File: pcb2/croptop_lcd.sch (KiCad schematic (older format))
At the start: 110 parts, among them J5 D.N.P., J6 686104183422, J7 62684-402100ALF, Q1 BSS138, Q2 BSS138, U11 TPD4E1U06, U12 FT812Q, U13 TPD4E1U06, U14 TPD4E1U06, U15 TPD4E1U06, U16 TPD4E1U06, U17 TPD4E1U06, U18 TPD4E1U06, U19 TPD4E1U06, U20 TPD4E1U06, Y2 ABLS-12.000MHZ-B2-T

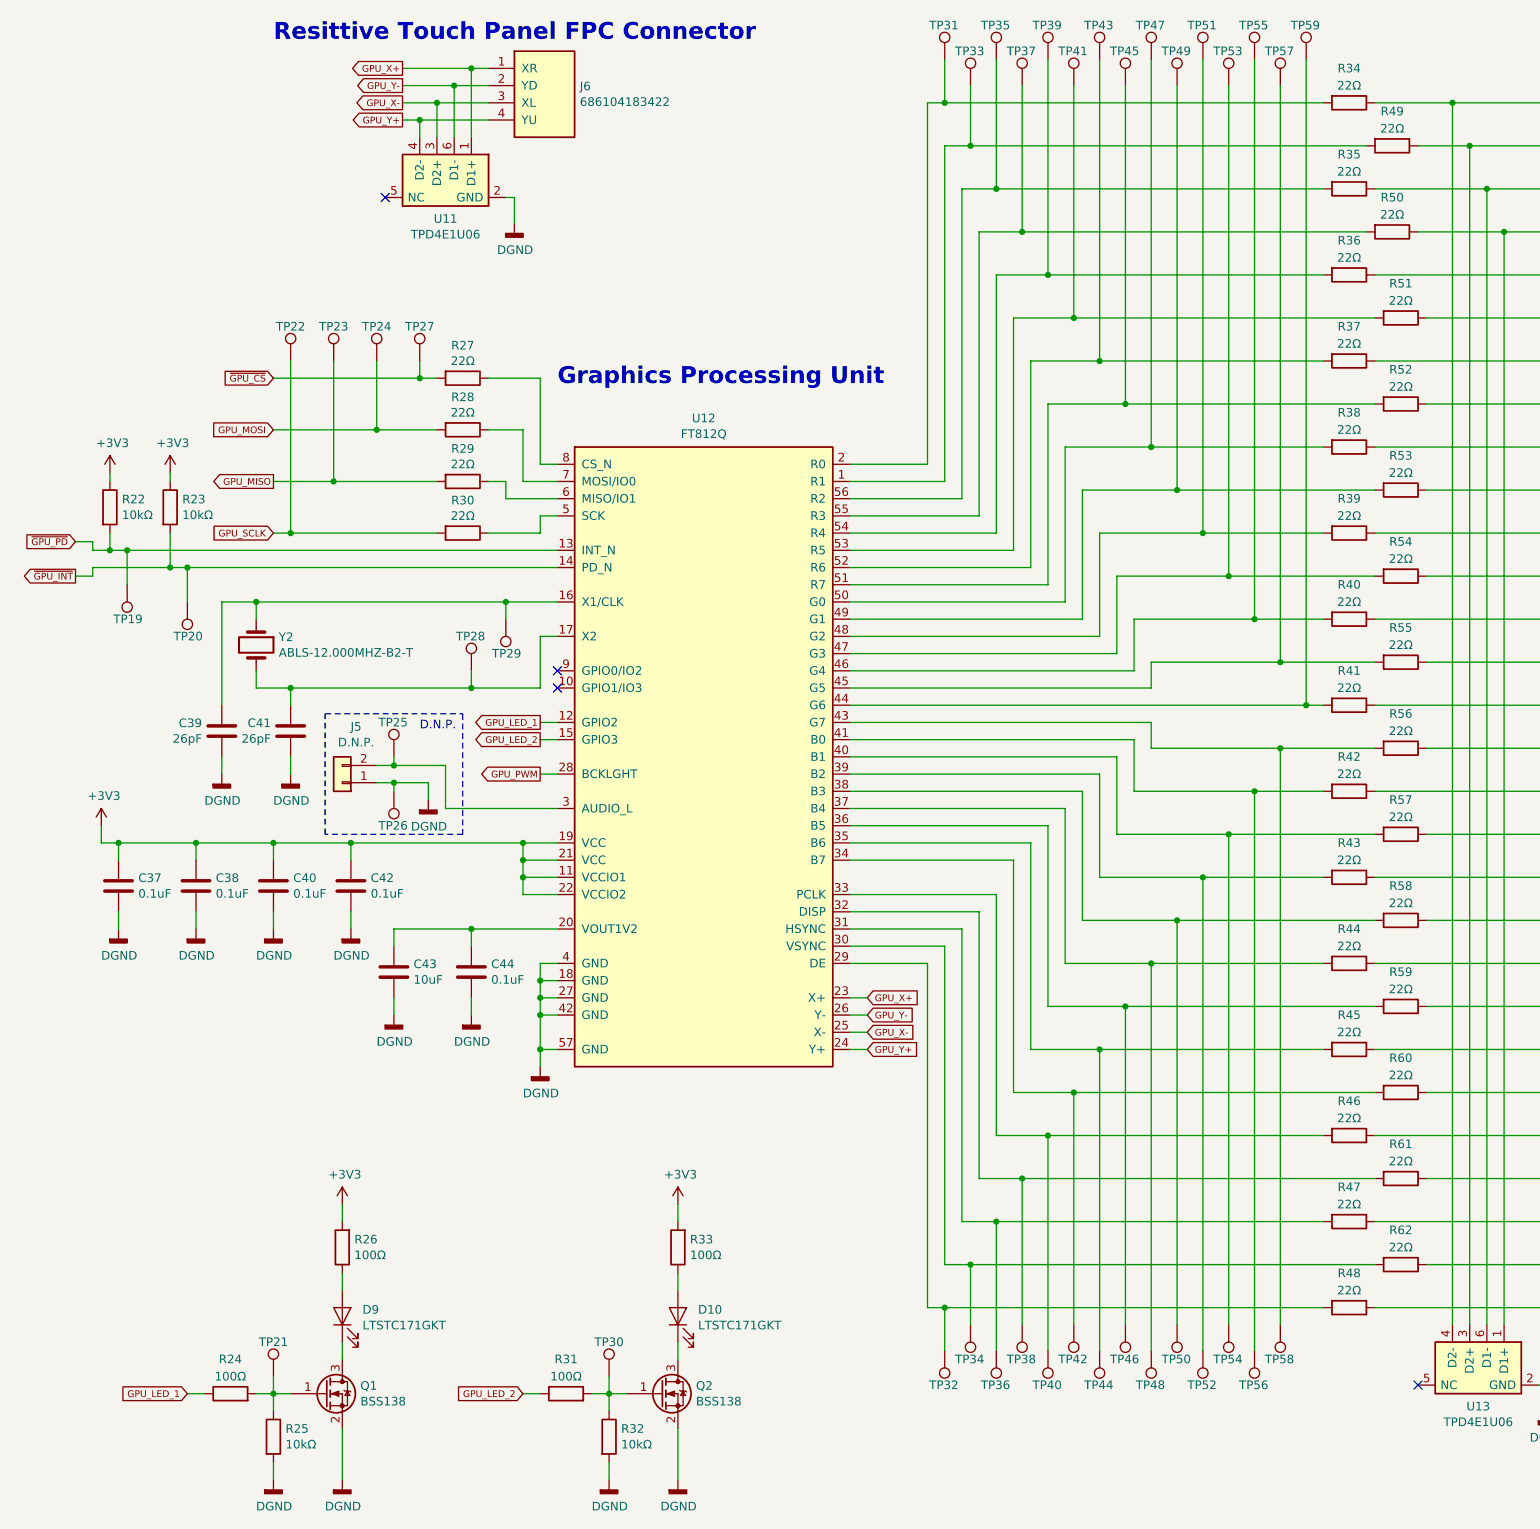
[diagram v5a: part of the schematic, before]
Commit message: Updated pin out
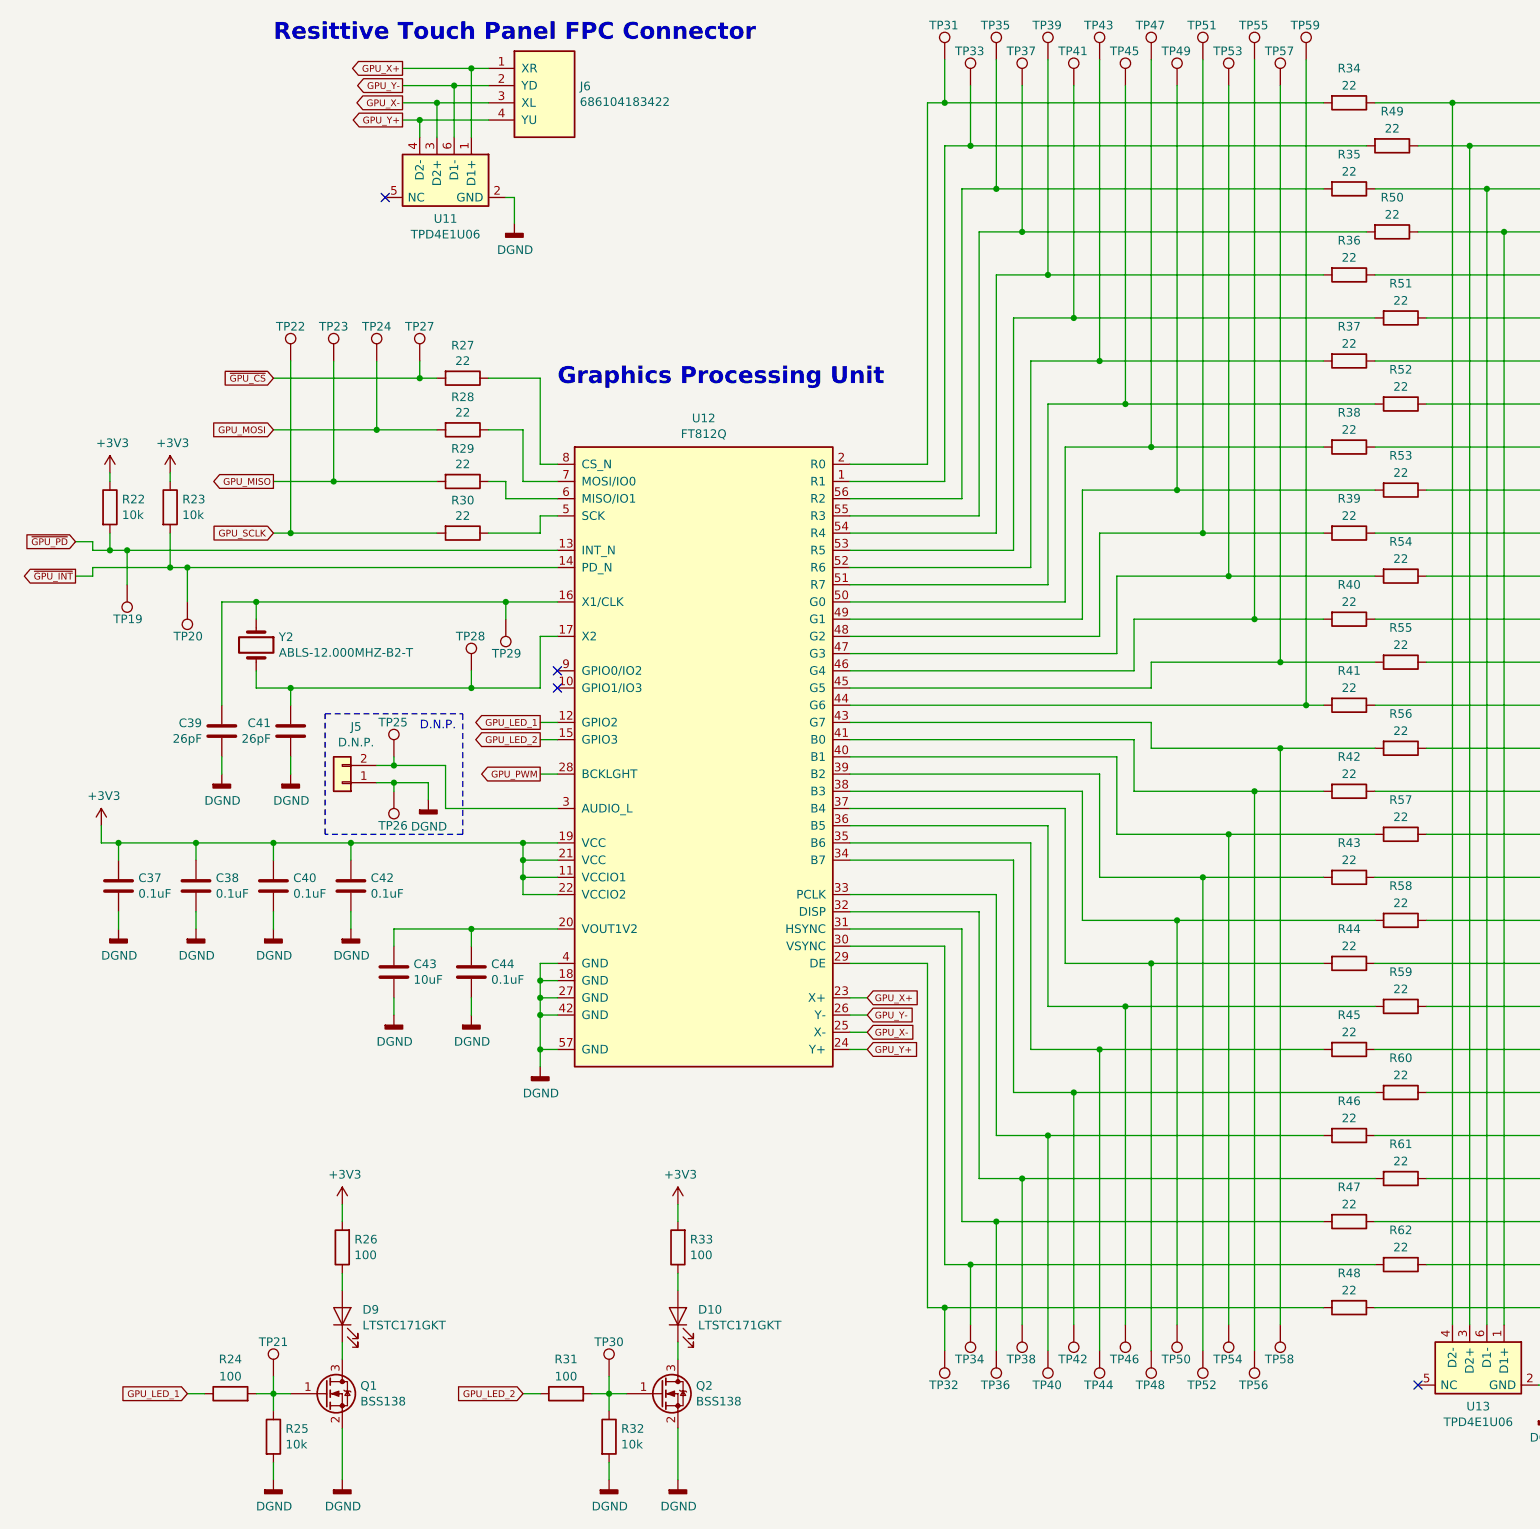
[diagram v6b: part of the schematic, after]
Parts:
- R22, R23, R25, R32: value 10kΩ -> 10k
- R24, R26, R31, R33: value 100Ω -> 100
- R27, R28, R29, R30, R34, R35, R36, R37, R38, R39, R40, R41, R42, R43, R44, R45, R46, R47, R48, R49, R50, R51, R52, R53, R54, R55, R56, R57, R58, R59, R60, R61, R62: value 22Ω -> 22
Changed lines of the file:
@@
 $Descr USLedger 17000 11000
 encoding utf-8
-Sheet 4 6
+Sheet 3 5
 Title "CropTop 2.0"
 Date "2019-03-18"
@@
 P 1150 3850
 F 0 "R22" H 1220 3896 50  0000 L CNN
-F 1 "10kΩ" H 1220 3805 50  0000 L CNN
+F 1 "10k" H 1220 3805 50  0000 L CNN
 F 2 "Resistor_SMD:R_0402_1005Metric" V 1080 3850 50  0001 C CNN
 F 3 "" H 1150 3850 50  0001 C CNN
@@
 P 1500 3850
 F 0 "R23" H 1570 3896 50  0000 L CNN
-F 1 "10kΩ" H 1570 3805 50  0000 L CNN
+F 1 "10k" H 1570 3805 50  0000 L CNN
 F 2 "Resistor_SMD:R_0402_1005Metric" V 1430 3850 50  0001 C CNN
 F 3 "" H 1500 3850 50  0001 C CNN
@@
 AR Path="/65B709D0/5CF1E28C" Ref="R30"  Part="1"
 F 0 "R30" V 3010 4000 50  0000 C CNN
-F 1 "22Ω" V 3100 4000 50  0000 C CNN
+F 1 "22" V 3100 4000 50  0000 C CNN
 F 2 "Resistor_SMD:R_0402_1005Metric" V 3130 4000 50  0001 C CNN
 F 3 "" H 3200 4000 50  0001 C CNN
@@
 AR Path="/65B709D0/5CF1E293" Ref="R29"  Part="1"
 F 0 "R29" V 3010 3700 50  0000 C CNN
-F 1 "22Ω" V 3100 3700 50  0000 C CNN
+F 1 "22" V 3100 3700 50  0000 C CNN
 F 2 "Resistor_SMD:R_0402_1005Metric" V 3130 3700 50  0001 C CNN
 F 3 "" H 3200 3700 50  0001 C CNN
@@
 AR Path="/65B709D0/5CF1E29A" Ref="R28"  Part="1"
 F 0 "R28" V 3010 3400 50  0000 C CNN
-F 1 "22Ω" V 3100 3400 50  0000 C CNN
+F 1 "22" V 3100 3400 50  0000 C CNN
 F 2 "Resistor_SMD:R_0402_1005Metric" V 3130 3400 50  0001 C CNN
 F 3 "" H 3200 3400 50  0001 C CNN
@@
 AR Path="/65B709D0/5CF1E2A1" Ref="R27"  Part="1"
 F 0 "R27" V 3010 3100 50  0000 C CNN
-F 1 "22Ω" V 3100 3100 50  0000 C CNN
+F 1 "22" V 3100 3100 50  0000 C CNN
 F 2 "Resistor_SMD:R_0402_1005Metric" V 3130 3100 50  0001 C CNN
 F 3 "" H 3200 3100 50  0001 C CNN
@@
 AR Path="/65B709D0/5F1C2A59" Ref="R26"  Part="1"
 F 0 "R26" H 2430 8104 50  0000 R CNN
-F 1 "100Ω" H 2430 8195 50  0000 R CNN
+F 1 "100" H 2430 8195 50  0000 R CNN
 F 2 "Resistor_SMD:R_0402_1005Metric" V 2430 8150 50  0001 C CNN
 F 3 "" H 2500 8150 50  0001 C CNN
@@
 AR Path="/65B709D0/5F1C2A67" Ref="R24"  Part="1"
 F 0 "R24" V 2050 9000 50  0000 C CNN
-F 1 "100Ω" V 1950 9000 50  0000 C CNN
+F 1 "100" V 1950 9000 50  0000 C CNN
 F 2 "Resistor_SMD:R_0402_1005Metric" V 1780 9000 50  0001 C CNN
 F 3 "" H 1850 9000 50  0001 C CNN
@@
 AR Path="/65B709D0/5F1C2A6E" Ref="R25"  Part="1"
 F 0 "R25" H 2170 9296 50  0000 L CNN
-F 1 "10kΩ" H 2170 9205 50  0000 L CNN
+F 1 "10k" H 2170 9205 50  0000 L CNN
 F 2 "Resistor_SMD:R_0402_1005Metric" V 2030 9250 50  0001 C CNN
 F 3 "" H 2100 9250 50  0001 C CNN
@@
 AR Path="/65B709D0/5F1ED0AE" Ref="R33"  Part="1"
 F 0 "R33" H 4380 8104 50  0000 R CNN
-F 1 "100Ω" H 4380 8195 50  0000 R CNN
+F 1 "100" H 4380 8195 50  0000 R CNN
 F 2 "Resistor_SMD:R_0402_1005Metric" V 4380 8150 50  0001 C CNN
 F 3 "" H 4450 8150 50  0001 C CNN
@@
 AR Path="/65B709D0/5F1ED0BC" Ref="R31"  Part="1"
 F 0 "R31" V 4000 9000 50  0000 C CNN
-F 1 "100Ω" V 3900 9000 50  0000 C CNN
+F 1 "100" V 3900 9000 50  0000 C CNN
 F 2 "Resistor_SMD:R_0402_1005Metric" V 3730 9000 50  0001 C CNN
 F 3 "" H 3800 9000 50  0001 C CNN
@@
 AR Path="/65B709D0/5F1ED0C3" Ref="R32"  Part="1"
 F 0 "R32" H 4120 9296 50  0000 L CNN
-F 1 "10kΩ" H 4120 9205 50  0000 L CNN
+F 1 "10k" H 4120 9205 50  0000 L CNN
 F 2 "Resistor_SMD:R_0402_1005Metric" V 3980 9250 50  0001 C CNN
 F 3 "" H 4050 9250 50  0001 C CNN
@@
 P 8350 1500
 F 0 "R34" V 8150 1500 50  0000 C CNN
-F 1 "22Ω" V 8250 1500 50  0000 C CNN
+F 1 "22" V 8250 1500 50  0000 C CNN
 F 2 "Resistor_SMD:R_0402_1005Metric" V 8280 1500 50  0001 C CNN
 F 3 "" H 8350 1500 50  0001 C CNN
@@
 P 8350 2500
 F 0 "R36" V 8150 2500 50  0000 C CNN
-F 1 "22Ω" V 8250 2500 50  0000 C CNN
+F 1 "22" V 8250 2500 50  0000 C CNN
 F 2 "Resistor_SMD:R_0402_1005Metric" V 8280 2500 50  0001 C CNN
 F 3 "" H 8350 2500 50  0001 C CNN
@@
 P 8600 2250
 F 0 "R50" V 8400 2250 50  0000 C CNN
-F 1 "22Ω" V 8500 2250 50  0000 C CNN
+F 1 "22" V 8500 2250 50  0000 C CNN
 F 2 "Resistor_SMD:R_0402_1005Metric" V 8530 2250 50  0001 C CNN
 F 3 "" H 8600 2250 50  0001 C CNN
@@
 P 8350 2000
 F 0 "R35" V 8150 2000 50  0000 C CNN
-F 1 "22Ω" V 8250 2000 50  0000 C CNN
+F 1 "22" V 8250 2000 50  0000 C CNN
 F 2 "Resistor_SMD:R_0402_1005Metric" V 8280 2000 50  0001 C CNN
 F 3 "" H 8350 2000 50  0001 C CNN
@@
 P 8600 1750
 F 0 "R49" V 8400 1750 50  0000 C CNN
-F 1 "22Ω" V 8500 1750 50  0000 C CNN
+F 1 "22" V 8500 1750 50  0000 C CNN
 F 2 "Resistor_SMD:R_0402_1005Metric" V 8530 1750 50  0001 C CNN
 F 3 "" H 8600 1750 50  0001 C CNN
@@
 P 8350 3500
 F 0 "R38" V 8150 3500 50  0000 C CNN
-F 1 "22Ω" V 8250 3500 50  0000 C CNN
+F 1 "22" V 8250 3500 50  0000 C CNN
 F 2 "Resistor_SMD:R_0402_1005Metric" V 8280 3500 50  0001 C CNN
 F 3 "" H 8350 3500 50  0001 C CNN
@@
 P 8650 3250
 F 0 "R52" V 8450 3250 50  0000 C CNN
-F 1 "22Ω" V 8550 3250 50  0000 C CNN
+F 1 "22" V 8550 3250 50  0000 C CNN
 F 2 "Resistor_SMD:R_0402_1005Metric" V 8580 3250 50  0001 C CNN
 F 3 "" H 8650 3250 50  0001 C CNN
@@
 P 8350 3000
 F 0 "R37" V 8150 3000 50  0000 C CNN
-F 1 "22Ω" V 8250 3000 50  0000 C CNN
+F 1 "22" V 8250 3000 50  0000 C CNN
 F 2 "Resistor_SMD:R_0402_1005Metric" V 8280 3000 50  0001 C CNN
 F 3 "" H 8350 3000 50  0001 C CNN
@@
 P 8650 2750
 F 0 "R51" V 8450 2750 50  0000 C CNN
-F 1 "22Ω" V 8550 2750 50  0000 C CNN
+F 1 "22" V 8550 2750 50  0000 C CNN
 F 2 "Resistor_SMD:R_0402_1005Metric" V 8580 2750 50  0001 C CNN
 F 3 "" H 8650 2750 50  0001 C CNN
@@
 P 8350 4500
 F 0 "R40" V 8150 4500 50  0000 C CNN
-F 1 "22Ω" V 8250 4500 50  0000 C CNN
+F 1 "22" V 8250 4500 50  0000 C CNN
 F 2 "Resistor_SMD:R_0402_1005Metric" V 8280 4500 50  0001 C CNN
 F 3 "" H 8350 4500 50  0001 C CNN
@@
 P 8650 4250
 F 0 "R54" V 8450 4250 50  0000 C CNN
-F 1 "22Ω" V 8550 4250 50  0000 C CNN
+F 1 "22" V 8550 4250 50  0000 C CNN
 F 2 "Resistor_SMD:R_0402_1005Metric" V 8580 4250 50  0001 C CNN
 F 3 "" H 8650 4250 50  0001 C CNN
@@
 P 8350 4000
 F 0 "R39" V 8150 4000 50  0000 C CNN
-F 1 "22Ω" V 8250 4000 50  0000 C CNN
+F 1 "22" V 8250 4000 50  0000 C CNN
 F 2 "Resistor_SMD:R_0402_1005Metric" V 8280 4000 50  0001 C CNN
 F 3 "" H 8350 4000 50  0001 C CNN
@@
 P 8650 3750
 F 0 "R53" V 8450 3750 50  0000 C CNN
-F 1 "22Ω" V 8550 3750 50  0000 C CNN
+F 1 "22" V 8550 3750 50  0000 C CNN
 F 2 "Resistor_SMD:R_0402_1005Metric" V 8580 3750 50  0001 C CNN
 F 3 "" H 8650 3750 50  0001 C CNN
@@
 P 8350 5500
 F 0 "R42" V 8150 5500 50  0000 C CNN
-F 1 "22Ω" V 8250 5500 50  0000 C CNN
+F 1 "22" V 8250 5500 50  0000 C CNN
 F 2 "Resistor_SMD:R_0402_1005Metric" V 8280 5500 50  0001 C CNN
 F 3 "" H 8350 5500 50  0001 C CNN
@@
 P 8650 5250
 F 0 "R56" V 8450 5250 50  0000 C CNN
-F 1 "22Ω" V 8550 5250 50  0000 C CNN
+F 1 "22" V 8550 5250 50  0000 C CNN
 F 2 "Resistor_SMD:R_0402_1005Metric" V 8580 5250 50  0001 C CNN
 F 3 "" H 8650 5250 50  0001 C CNN
@@
 P 8350 5000
 F 0 "R41" V 8150 5000 50  0000 C CNN
-F 1 "22Ω" V 8250 5000 50  0000 C CNN
+F 1 "22" V 8250 5000 50  0000 C CNN
 F 2 "Resistor_SMD:R_0402_1005Metric" V 8280 5000 50  0001 C CNN
 F 3 "" H 8350 5000 50  0001 C CNN
@@
 P 8650 4750
 F 0 "R55" V 8450 4750 50  0000 C CNN
-F 1 "22Ω" V 8550 4750 50  0000 C CNN
+F 1 "22" V 8550 4750 50  0000 C CNN
 F 2 "Resistor_SMD:R_0402_1005Metric" V 8580 4750 50  0001 C CNN
 F 3 "" H 8650 4750 50  0001 C CNN
@@
 P 8350 6500
 F 0 "R44" V 8150 6500 50  0000 C CNN
-F 1 "22Ω" V 8250 6500 50  0000 C CNN
+F 1 "22" V 8250 6500 50  0000 C CNN
 F 2 "Resistor_SMD:R_0402_1005Metric" V 8280 6500 50  0001 C CNN
 F 3 "" H 8350 6500 50  0001 C CNN
@@
 P 8650 6250
 F 0 "R58" V 8450 6250 50  0000 C CNN
-F 1 "22Ω" V 8550 6250 50  0000 C CNN
+F 1 "22" V 8550 6250 50  0000 C CNN
 F 2 "Resistor_SMD:R_0402_1005Metric" V 8580 6250 50  0001 C CNN
 F 3 "" H 8650 6250 50  0001 C CNN
@@
 P 8350 6000
 F 0 "R43" V 8150 6000 50  0000 C CNN
-F 1 "22Ω" V 8250 6000 50  0000 C CNN
+F 1 "22" V 8250 6000 50  0000 C CNN
 F 2 "Resistor_SMD:R_0402_1005Metric" V 8280 6000 50  0001 C CNN
 F 3 "" H 8350 6000 50  0001 C CNN
@@
 P 8650 5750
 F 0 "R57" V 8450 5750 50  0000 C CNN
-F 1 "22Ω" V 8550 5750 50  0000 C CNN
+F 1 "22" V 8550 5750 50  0000 C CNN
 F 2 "Resistor_SMD:R_0402_1005Metric" V 8580 5750 50  0001 C CNN
 F 3 "" H 8650 5750 50  0001 C CNN
@@
 P 8350 7500
 F 0 "R46" V 8150 7500 50  0000 C CNN
-F 1 "22Ω" V 8250 7500 50  0000 C CNN
+F 1 "22" V 8250 7500 50  0000 C CNN
 F 2 "Resistor_SMD:R_0402_1005Metric" V 8280 7500 50  0001 C CNN
 F 3 "" H 8350 7500 50  0001 C CNN
@@
 P 8650 7250
 F 0 "R60" V 8450 7250 50  0000 C CNN
-F 1 "22Ω" V 8550 7250 50  0000 C CNN
+F 1 "22" V 8550 7250 50  0000 C CNN
 F 2 "Resistor_SMD:R_0402_1005Metric" V 8580 7250 50  0001 C CNN
 F 3 "" H 8650 7250 50  0001 C CNN
@@
 P 8350 7000
 F 0 "R45" V 8150 7000 50  0000 C CNN
-F 1 "22Ω" V 8250 7000 50  0000 C CNN
+F 1 "22" V 8250 7000 50  0000 C CNN
 F 2 "Resistor_SMD:R_0402_1005Metric" V 8280 7000 50  0001 C CNN
 F 3 "" H 8350 7000 50  0001 C CNN
@@
 P 8650 6750
 F 0 "R59" V 8450 6750 50  0000 C CNN
-F 1 "22Ω" V 8550 6750 50  0000 C CNN
+F 1 "22" V 8550 6750 50  0000 C CNN
 F 2 "Resistor_SMD:R_0402_1005Metric" V 8580 6750 50  0001 C CNN
 F 3 "" H 8650 6750 50  0001 C CNN
@@
 P 8350 8500
 F 0 "R48" V 8150 8500 50  0000 C CNN
-F 1 "22Ω" V 8250 8500 50  0000 C CNN
+F 1 "22" V 8250 8500 50  0000 C CNN
 F 2 "Resistor_SMD:R_0402_1005Metric" V 8280 8500 50  0001 C CNN
 F 3 "" H 8350 8500 50  0001 C CNN
@@
 P 8650 8250
 F 0 "R62" V 8450 8250 50  0000 C CNN
-F 1 "22Ω" V 8550 8250 50  0000 C CNN
+F 1 "22" V 8550 8250 50  0000 C CNN
 F 2 "Resistor_SMD:R_0402_1005Metric" V 8580 8250 50  0001 C CNN
 F 3 "" H 8650 8250 50  0001 C CNN
@@
 P 8350 8000
 F 0 "R47" V 8150 8000 50  0000 C CNN
-F 1 "22Ω" V 8250 8000 50  0000 C CNN
+F 1 "22" V 8250 8000 50  0000 C CNN
 F 2 "Resistor_SMD:R_0402_1005Metric" V 8280 8000 50  0001 C CNN
 F 3 "" H 8350 8000 50  0001 C CNN
@@
 P 8650 7750
 F 0 "R61" V 8450 7750 50  0000 C CNN
-F 1 "22Ω" V 8550 7750 50  0000 C CNN
+F 1 "22" V 8550 7750 50  0000 C CNN
 F 2 "Resistor_SMD:R_0402_1005Metric" V 8580 7750 50  0001 C CNN
 F 3 "" H 8650 7750 50  0001 C CNN
